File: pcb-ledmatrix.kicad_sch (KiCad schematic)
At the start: 45 parts, among them J1 USB_C_Receptacle_USB2.0_16P, J2 Conn_01x04_Pin, J3 Conn_01x04_Pin, J4 Conn_01x04_Pin, Q1 SS8050, SW1 SW_Push, SW2 SW_Push, U1 USBLC6-2SC6, U2 ESP32-C3-WROOM-02, U3 SPX3819M5-L-3-3, Y1 32.768kHz

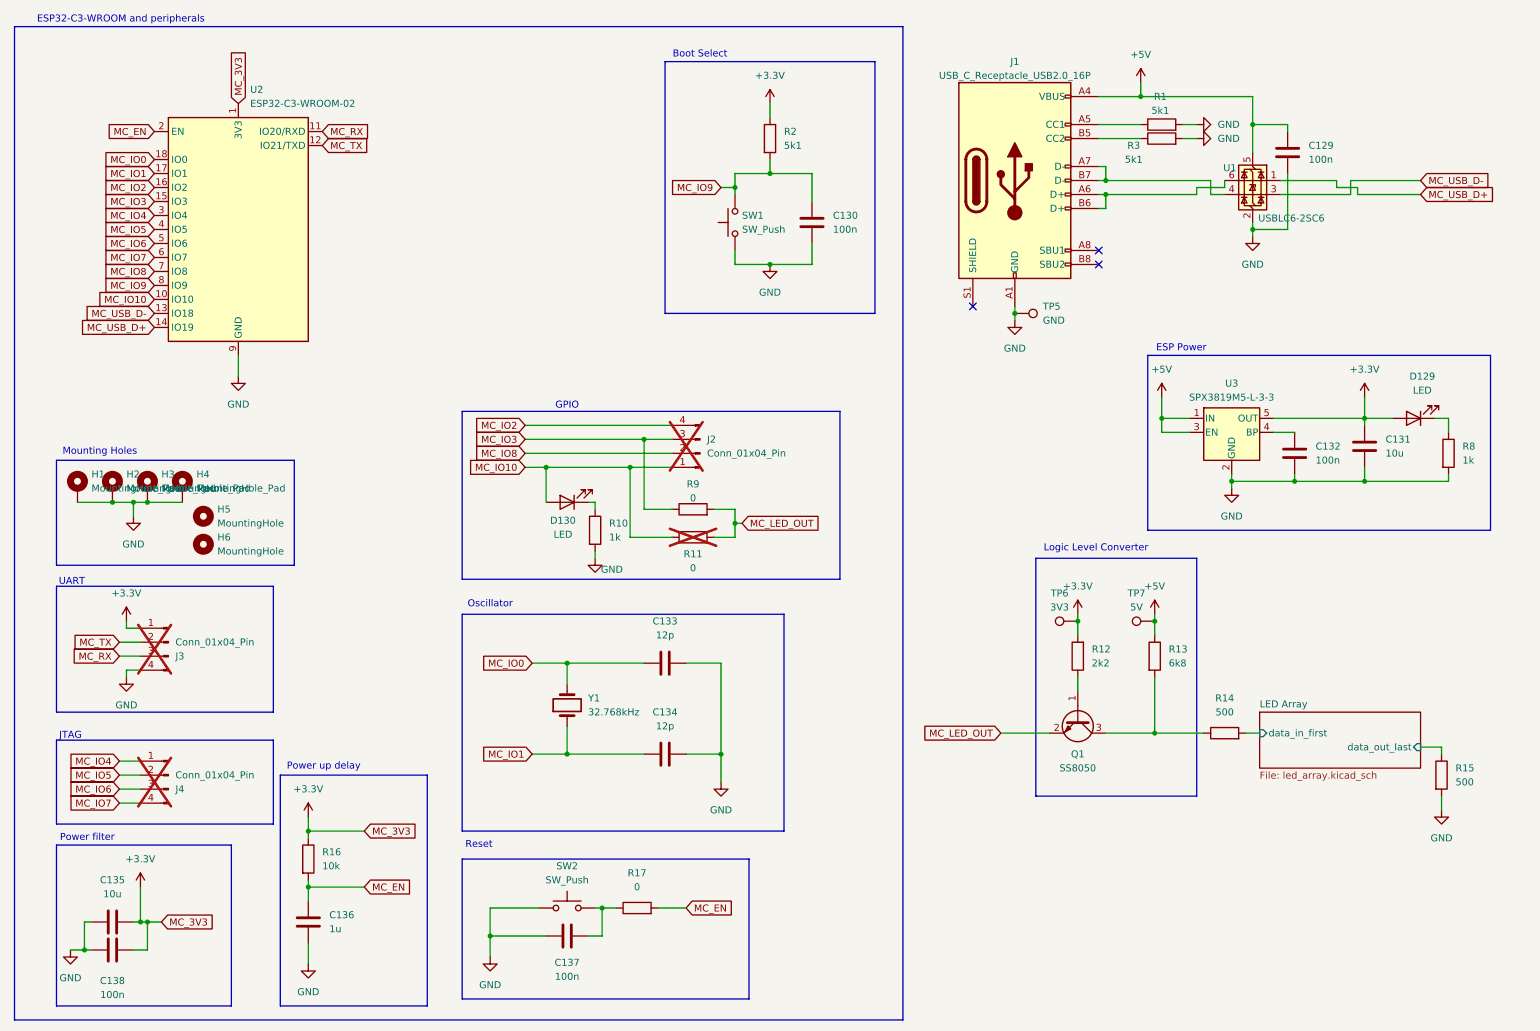
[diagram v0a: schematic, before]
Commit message: change level shifter in schematic
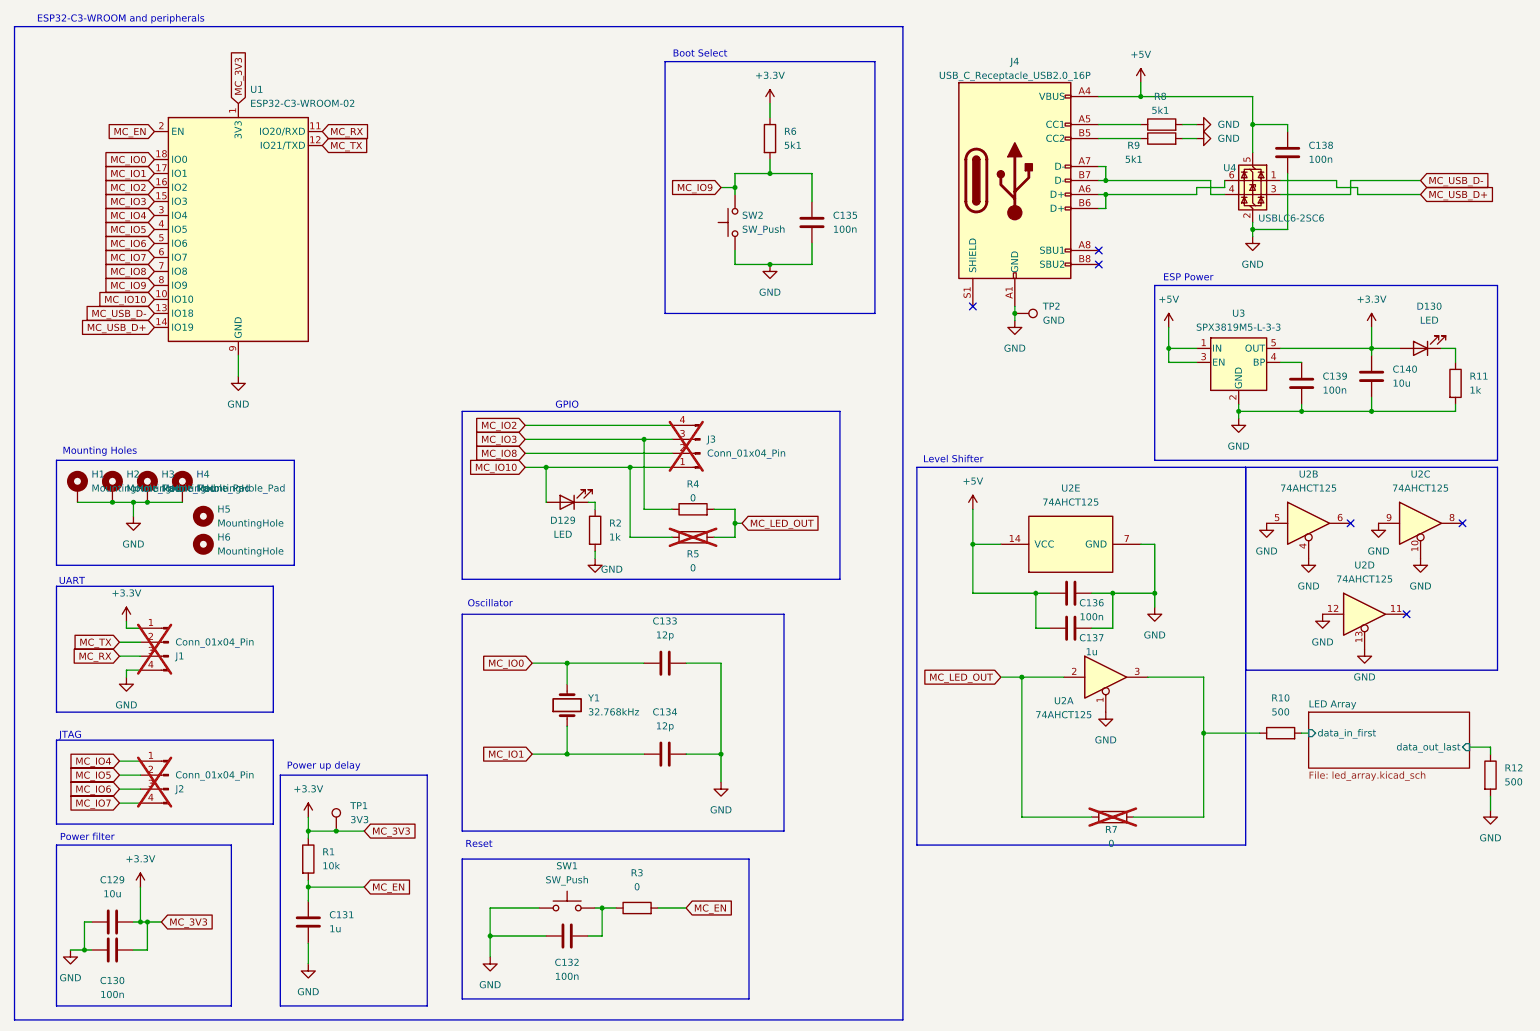
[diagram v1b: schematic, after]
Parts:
- removed Q1: SS8050, Package_TO_SOT_SMD:SOT-23, symbol Transistor_BJT:SS8050
- removed R12: 2k2, Resistor_SMD:R_0603_1608Metric, symbol Device:R
- removed R13: 6k8, Resistor_SMD:R_0603_1608Metric, symbol Device:R
- removed TP7: 5V, TestPoint:TestPoint_Pad_2.0x2.0mm, symbol Connector:TestPoint
- added C136: 100n, Capacitor_SMD:C_0603_1608Metric, symbol Device:C
- added C137: 1u, Capacitor_SMD:C_0603_1608Metric, symbol Device:C
- added R7: 0, Resistor_SMD:R_0603_1608Metric, symbol Device:R
- added U2: 74AHCT125, Package_SO:SOIC-14_3.9x8.7mm_P1.27mm, symbol 74xx:74AHCT125
- renumbered C135 to C129, C138 to C130, C136 to C131, C137 to C132, C130 to C135, C129 to C138, C132 to C139, C131 to C140, D130 to D129, D129 to D130, J3 to J1, J4 to J2, J2 to J3, J1 to J4, R16 to R1, R14 to R10, R8 to R11, R15 to R12, R10 to R2, R17 to R3, R9 to R4, R11 to R5, R2 to R6, R1 to R8, R3 to R9, SW2 to SW1, SW1 to SW2, TP6 to TP1, TP5 to TP2, U2 to U1, U1 to U4
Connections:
- net +5V: now also C136.1, C137.1, U2.14 (VCC)
- net GND: now also C136.2, C137.2, U2.1, U2.10, U2.12, U2.13, U2.4, U2.5, U2.7 (GND), U2.9
- net MC_LED_OUT: now also R7.1, U2.2
- net at R10.1: now also R7.2, U2.3
- no-connect marks 3 -> 6
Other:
- note added: "Level Shifter"
- note removed: "Logic Level Converter"
- moved on the sheet: C139, C140, D130, R10, R11, R12, TP1, U3

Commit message: finisch layout, add prod files
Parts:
- added R13: 0, Resistor_SMD:R_0603_1608Metric, symbol Device:R
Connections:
- net at R10.1, R7.2: now also R13.2; no longer U2.3
- new net: R13.1, U2.3
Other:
- moved on the sheet: R7, U2A
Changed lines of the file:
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@@
 	)
 	(junction
-		(at 31.75 102.87)
+		(at 231.14 144.78)
 		(diameter 0)
 		(color 0 0 0 0)
 	)
 	(junction
-		(at 199.39 119.38)
+		(at 31.75 102.87)
 		(diameter 0)
 		(color 0 0 0 0)
 	)
 	(junction
-		(at 229.87 144.78)
+		(at 199.39 119.38)
 		(diameter 0)
 		(color 0 0 0 0)
@@
 	)
 	(junction
-		(at 196.85 134.62)
+		(at 196.85 139.7)
 		(diameter 0)
 		(color 0 0 0 0)
@@
 	(wire
 		(pts
-			(xy 193.04 134.62) (xy 196.85 134.62)
+			(xy 193.04 139.7) (xy 196.85 139.7)
 		)
 		(stroke
@@
 	(wire
 		(pts
-			(xy 229.87 144.78) (xy 229.87 160.02)
-		)
-		(stroke
-			(width 0)
-			(type default)
-		)
-	)
-	(wire
-		(pts
 			(xy 72.39 162.56) (xy 77.47 162.56)
 		)
@@
 	(wire
 		(pts
-			(xy 209.55 160.02) (xy 196.85 160.02)
+			(xy 209.55 156.21) (xy 196.85 156.21)
 		)
 		(stroke
@@
 	(wire
 		(pts
+			(xy 231.14 144.78) (xy 231.14 156.21)
+		)
+		(stroke
+			(width 0)
+			(type default)
+		)
+	)
+	(wire
+		(pts
 			(xy 36.83 179.07) (xy 38.1 179.07)
 		)
@@
 	(wire
 		(pts
-			(xy 196.85 134.62) (xy 204.47 134.62)
+			(xy 196.85 139.7) (xy 204.47 139.7)
 		)
 		(stroke
@@
 	(wire
 		(pts
-			(xy 219.71 134.62) (xy 229.87 134.62)
-		)
-		(stroke
-			(width 0)
-			(type default)
-		)
-	)
-	(wire
-		(pts
 			(xy 236.22 85.09) (xy 236.22 86.36)
 		)
@@
 	(wire
 		(pts
-			(xy 196.85 134.62) (xy 196.85 160.02)
+			(xy 196.85 139.7) (xy 196.85 156.21)
 		)
 		(stroke
@@
 	(wire
 		(pts
-			(xy 229.87 144.78) (xy 240.03 144.78)
+			(xy 231.14 144.78) (xy 240.03 144.78)
 		)
 		(stroke
@@
 	(wire
 		(pts
-			(xy 217.17 160.02) (xy 229.87 160.02)
+			(xy 217.17 156.21) (xy 231.14 156.21)
 		)
 		(stroke
@@
 	(wire
 		(pts
-			(xy 229.87 134.62) (xy 229.87 144.78)
+			(xy 231.14 139.7) (xy 231.14 144.78)
 		)
 		(stroke
@@
 	(wire
 		(pts
+			(xy 219.71 139.7) (xy 222.25 139.7)
+		)
+		(stroke
+			(width 0)
+			(type default)
+		)
+	)
+	(wire
+		(pts
 			(xy 35.56 179.07) (xy 36.83 179.07)
 		)
@@
 	(wire
 		(pts
+			(xy 231.14 139.7) (xy 229.87 139.7)
+		)
+		(stroke
+			(width 0)
+			(type default)
+		)
+	)
+	(wire
+		(pts
 			(xy 67.31 182.88) (xy 67.31 186.69)
 		)
@@
 	(global_label "MC_LED_OUT"
 		(shape input)
-		(at 193.04 134.62 180)
+		(at 193.04 139.7 180)
 		(fields_autoplaced yes)
 		(effects
@@
 		)
 		(property "Intersheetrefs" "${INTERSHEET_REFS}"
-			(at 178.3225 134.62 0)
+			(at 178.3225 139.7 0)
 			(effects
 				(font
@@
 	(symbol
 		(lib_id "74xx:74AHCT125")
-		(at 212.09 134.62 0)
+		(at 212.09 139.7 0)
 		(unit 1)
 		(exclude_from_sim no)
@@
 		(dnp no)
 		(property "Reference" "U2"
-			(at 204.47 138.938 0)
+			(at 204.47 144.018 0)
 			(effects
 				(font
@@
 		)
 		(property "Value" "74AHCT125"
-			(at 204.47 141.478 0)
+			(at 204.47 146.558 0)
 			(effects
 				(font
@@
 		)
 		(property "Footprint" "Package_SO:SOIC-14_3.9x8.7mm_P1.27mm"
-			(at 212.09 134.62 0)
+			(at 212.09 139.7 0)
 			(effects
 				(font
@@
 		)
 		(property "Datasheet" "https://www.ti.com/lit/ds/symlink/sn74ahct125.pdf"
-			(at 212.09 134.62 0)
+			(at 212.09 139.7 0)
 			(effects
 				(font
@@
 		)
 		(property "Description" "Quadruple Bus Buffer Gates With 3-State Outputs"
-			(at 212.09 134.62 0)
+			(at 212.09 139.7 0)
 			(effects
 				(font
@@
 		)
 		(property "JLCPCB Part" "C155176"
-			(at 212.09 134.62 0)
+			(at 212.09 139.7 0)
 			(effects
 				(font
@@
 	)
 	(symbol
+		(lib_id "Device:R")
+		(at 226.06 139.7 90)
+		(unit 1)
+		(exclude_from_sim no)
+		(in_bom yes)
+		(on_board yes)
+		(dnp no)
+		(property "Reference" "R13"
+			(at 225.806 141.986 90)
+			(effects
+				(font
+					(size 1.27 1.27)
+				)
+			)
+		)
+		(property "Value" "0"
+			(at 225.806 144.526 90)
+			(effects
+				(font
+					(size 1.27 1.27)
+				)
+			)
+		)
+		(property "Footprint" "Resistor_SMD:R_0603_1608Metric"
+			(at 226.06 141.478 90)
+			(effects
+				(font
+					(size 1.27 1.27)
+				)
+				(hide yes)
+			)
+		)
+		(property "Datasheet" "~"
+			(at 226.06 139.7 0)
+			(effects
+				(font
+					(size 1.27 1.27)
+				)
+				(hide yes)
+			)
+		)
+		(property "Description" "Resistor"
+			(at 226.06 139.7 0)
+			(effects
+				(font
+					(size 1.27 1.27)
+				)
+				(hide yes)
+			)
+		)
+		(pin "2"
+		)
+		(pin "1"
+		)
+		(instances
+			(project "pcb-ledmatrix"
+				(path "/88049e7b-1218-4b3d-b2ce-dbc2b6460fd5"
+					(reference "R13")
+					(unit 1)
+				)
+			)
+		)
+	)
+	(symbol
 		(lib_id "power:+3.3V")
 		(at 151.13 30.48 0)
@@
 	(symbol
 		(lib_id "power:GND")
-		(at 212.09 140.97 0)
+		(at 212.09 146.05 0)
 		(unit 1)
 		(exclude_from_sim no)
@@
 		(fields_autoplaced yes)
 		(property "Reference" "#PWR0287"
-			(at 212.09 147.32 0)
+			(at 212.09 152.4 0)
 			(effects
 				(font
@@
 		)
 		(property "Value" "GND"
-			(at 212.09 146.05 0)
+			(at 212.09 151.13 0)
 			(effects
 				(font
@@
 		)
 		(property "Footprint" ""
-			(at 212.09 140.97 0)
+			(at 212.09 146.05 0)
 			(effects
 				(font
@@
 		)
 		(property "Datasheet" ""
-			(at 212.09 140.97 0)
+			(at 212.09 146.05 0)
 			(effects
 				(font
@@
 		)
 		(property "Description" "Power symbol creates a global label with name \"GND\" , ground"
-			(at 212.09 140.97 0)
+			(at 212.09 146.05 0)
 			(effects
 				(font
@@
 	(symbol
 		(lib_id "Device:R")
-		(at 213.36 160.02 90)
+		(at 213.36 156.21 90)
 		(unit 1)
 		(exclude_from_sim no)
@@
 		(dnp yes)
 		(property "Reference" "R7"
-			(at 213.106 162.306 90)
+			(at 213.106 158.496 90)
 			(effects
 				(font
@@
 		)
 		(property "Value" "0"
-			(at 213.106 164.846 90)
+			(at 213.106 161.036 90)
 			(effects
 				(font
@@
 		)
 		(property "Footprint" "Resistor_SMD:R_0603_1608Metric"
-			(at 213.36 161.798 90)
+			(at 213.36 157.988 90)
 			(effects
 				(font
@@
 		)
 		(property "Datasheet" "~"
-			(at 213.36 160.02 0)
+			(at 213.36 156.21 0)
 			(effects
 				(font
@@
 		)
 		(property "Description" "Resistor"
-			(at 213.36 160.02 0)
+			(at 213.36 156.21 0)
 			(effects
 				(font
@@
 		)
 		(property "Value" "1u"
-			(at 209.55 130.048 90)
+			(at 209.55 135.128 90)
 			(effects
 				(font
